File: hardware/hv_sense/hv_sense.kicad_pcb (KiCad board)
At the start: 2 copper layers, 25 parts, among them J1 Conn_01x02, J2 Conn_01x04, U1 TLV274, U2 TL431ACDT, U3 140817141410, U4 140817141410

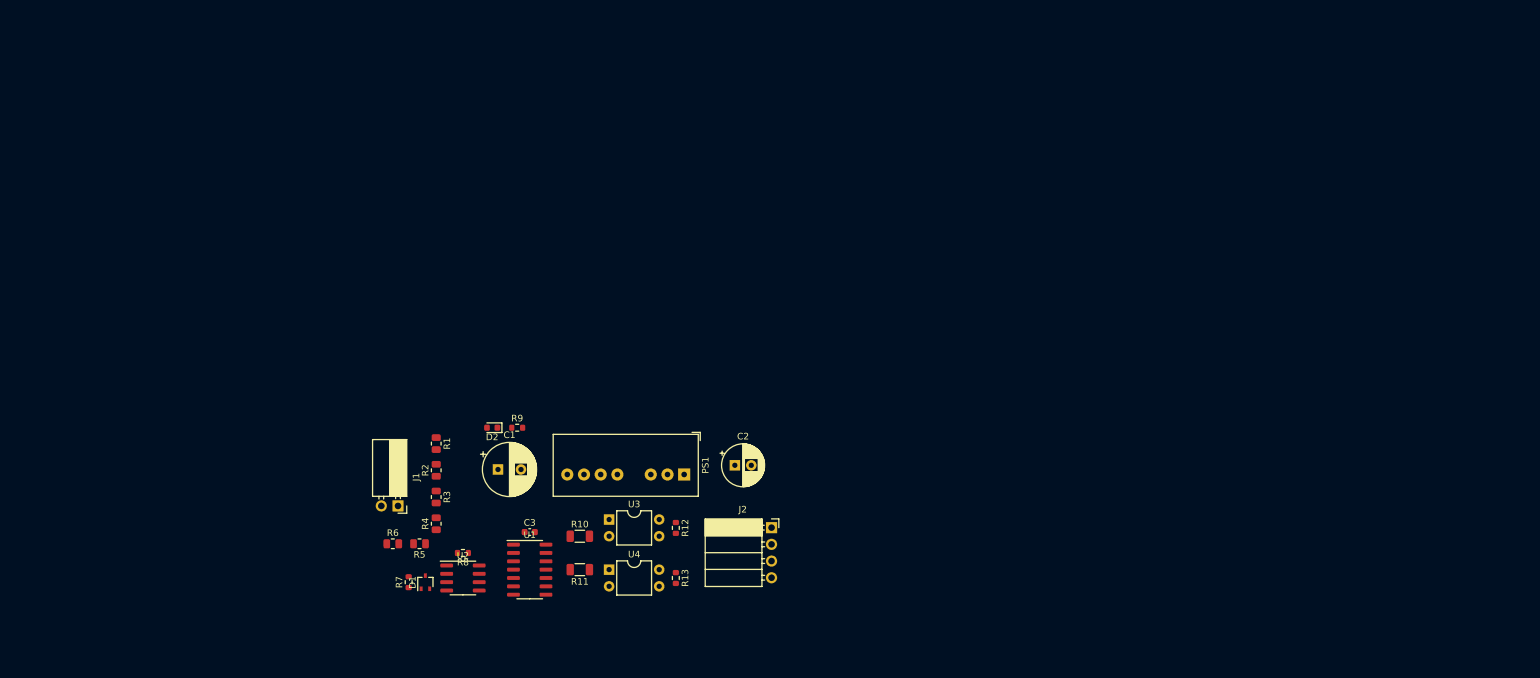
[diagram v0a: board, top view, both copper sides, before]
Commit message: Integrated TSAL logic into hv_sense
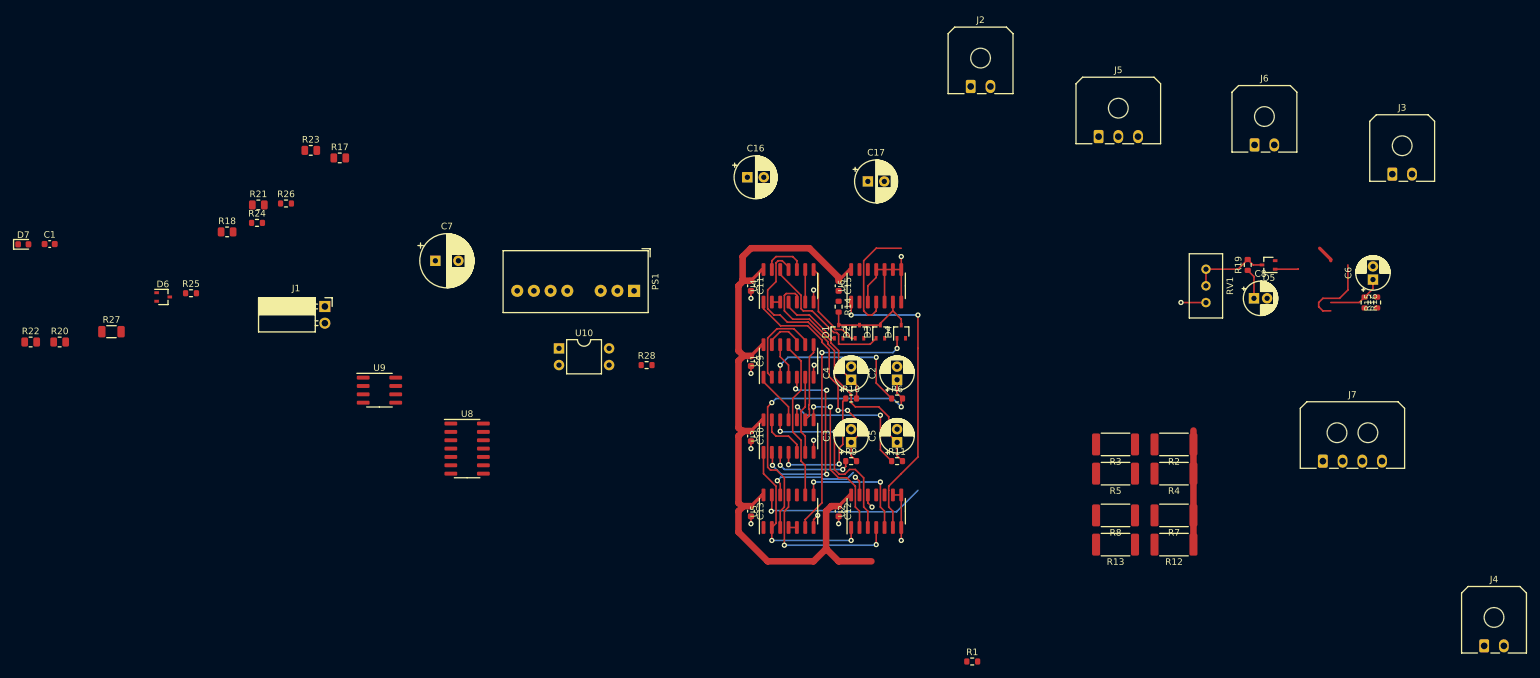
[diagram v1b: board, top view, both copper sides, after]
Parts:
- added C10: 100n, Capacitor_SMD:C_0603_1608Metric, F.Cu at (150.5, 78.1)
- added C11: 100n, Capacitor_SMD:C_0603_1608Metric, F.Cu at (150.5, 55.2)
- added C12: 100n, Capacitor_SMD:C_0603_1608Metric, F.Cu at (163.8, 89.5)
- added C13: 100n, Capacitor_SMD:C_0603_1608Metric, F.Cu at (150.5, 89.5)
- added C15: 100n, Capacitor_SMD:C_0603_1608Metric, F.Cu at (163.8, 55.2)
- added C16: 100u, Capacitor_THT:CP_Radial_D6.3mm_P2.50mm, F.Cu at (149.9, 38.7)
- added C17: 100u, Capacitor_THT:CP_Radial_D6.3mm_P2.50mm, F.Cu at (168.3, 39.4)
- added C4: 10u, Capacitor_THT:CP_Radial_D5.0mm_P2.00mm, F.Cu at (165.7, 69.5)
- added C5: 10u, Capacitor_THT:CP_Radial_D5.0mm_P2.00mm, F.Cu at (172.7, 79.1)
- added C6: 10u, Capacitor_THT:CP_Radial_D5.0mm_P2.00mm, F.Cu at (245.1, 54.3)
- added C7: 22u, Capacitor_THT:CP_Radial_D8.0mm_P3.50mm, F.Cu at (102.5, 51.4)
- added C8: 10u, Capacitor_THT:CP_Radial_D5.0mm_P2.00mm, F.Cu at (227.0, 57.1)
- added C9: 100n, Capacitor_SMD:C_0603_1608Metric, F.Cu at (150.5, 66.7)
- added D3: BAT54W, Package_TO_SOT_SMD:SOT-323_SC-70, F.Cu at (170.2, 62.2)
- added D4: BAT54W, Package_TO_SOT_SMD:SOT-323_SC-70, F.Cu at (173.4, 62.2)
- added D5: BAT54W, Package_TO_SOT_SMD:SOT-323_SC-70, F.Cu at (229.2, 52.1)
- added D6: BAT54W, Package_TO_SOT_SMD:SOT-323_SC-70, F.Cu at (61.1, 56.9)
- added D7: LED, LED_SMD:LED_0603_1608Metric, F.Cu at (39.8, 48.9)
- added J3: Conn_01x02, Connector_Molex:Molex_Micro-Fit_3.0_43650-0200_1x02_P3.00mm_Horizontal, F.Cu at (248.1, 38.3)
- added J4: Conn_01x02, Connector_Molex:Molex_Micro-Fit_3.0_43650-0200_1x02_P3.00mm_Horizontal, F.Cu at (262.0, 110.0)
- added J5: Conn_01x03, Connector_Molex:Molex_Micro-Fit_3.0_43650-0300_1x03_P3.00mm_Horizontal, F.Cu at (203.4, 32.5)
- added J6: Conn_01x02, Connector_Molex:Molex_Micro-Fit_3.0_43650-0200_1x02_P3.00mm_Horizontal, F.Cu at (227.1, 33.8)
- added J7: Conn_01x04, Connector_Molex:Molex_Micro-Fit_3.0_43650-0400_1x04_P3.00mm_Horizontal, F.Cu at (237.5, 81.9)
- added R14: 10k, Resistor_SMD:R_0603_1608Metric, F.Cu at (163.8, 58.4)
- added R15: 10k, Resistor_SMD:R_0603_1608Metric, F.Cu at (245.7, 57.8)
- added R16: 10k, Resistor_SMD:R_0603_1608Metric, F.Cu at (243.8, 57.8)
- added R17: 453k, Resistor_SMD:R_0805_2012Metric, F.Cu at (87.9, 35.8)
- added R18: 453k, Resistor_SMD:R_0805_2012Metric, F.Cu at (70.8, 47.0)
- added R19: 10k, Resistor_SMD:R_0603_1608Metric, F.Cu at (226.1, 52.1)
- added R20: 453k, Resistor_SMD:R_0805_2012Metric, F.Cu at (45.3, 63.8)
- added R21: 453k, Resistor_SMD:R_0805_2012Metric, F.Cu at (75.6, 42.9)
- added R22: 453k, Resistor_SMD:R_0805_2012Metric, F.Cu at (40.9, 63.8)
- added R23: 453k, Resistor_SMD:R_0805_2012Metric, F.Cu at (83.5, 34.6)
- added R24: 3.3k, Resistor_SMD:R_0603_1608Metric, F.Cu at (75.4, 45.7)
- added R25: 150k, Resistor_SMD:R_0603_1608Metric, F.Cu at (65.3, 56.4)
- added R26: 3.3k, Resistor_SMD:R_0603_1608Metric, F.Cu at (79.8, 42.7)
- added R27: 1k, Resistor_SMD:R_1206_3216Metric, F.Cu at (53.2, 62.2)
- added R28: 10k, Resistor_SMD:R_0603_1608Metric, F.Cu at (134.6, 67.3)
- added RV1: 470k, Potentiometer_THT:Potentiometer_Bourns_3296W_Vertical, F.Cu at (219.7, 57.8)
- added U10: 140817141410, Package_DIP:DIP-4_W7.62mm, F.Cu at (121.3, 64.8)
- added U5: 40106, Package_SO:SOIC-14_3.9x8.7mm_P1.27mm, F.Cu at (156.2, 89.5)
- added U6: 4013, Package_SO:SOIC-14_3.9x8.7mm_P1.27mm, F.Cu at (169.5, 55.2)
- added U8: TLV274, Package_SO:SOIC-14_3.9x8.7mm_P1.27mm, F.Cu at (107.3, 80.0)
- added U9: TL431ACDT, Package_SO:SOIC-8_3.9x4.9mm_P1.27mm, F.Cu at (94.0, 71.1)
- C1: value 22u -> 100n; footprint Capacitor_THT:CP_Radial_D8.0mm_P3.50mm -> Capacitor_SMD:C_0603_1608Metric
- C2: value 100u -> 10u; footprint Capacitor_THT:CP_Radial_D6.3mm_P2.50mm -> Capacitor_THT:CP_Radial_D5.0mm_P2.00mm
- C3: value 100n -> 10u; footprint Capacitor_SMD:C_0603_1608Metric -> Capacitor_THT:CP_Radial_D5.0mm_P2.00mm
- D2: value LED -> BAT54W; footprint LED_SMD:LED_0603_1608Metric -> Package_TO_SOT_SMD:SOT-323_SC-70
- J2: value Conn_01x04 -> Conn_01x02; footprint Connector_PinSocket_2.54mm:PinSocket_1x04_P2.54mm_Horizontal -> Connector_Molex:Molex_Micro-Fit_3.0_43650-0200_1x02_P3.00mm_Horizontal
- R1: value 453k -> 10k; footprint Resistor_SMD:R_0805_2012Metric -> Resistor_SMD:R_0603_1608Metric
- R10, R11: value 1k -> 10k; footprint Resistor_SMD:R_1206_3216Metric -> Resistor_SMD:R_0603_1608Metric
- R12, R13: value 10k -> 82; footprint Resistor_SMD:R_0603_1608Metric -> Resistor_SMD:R_2512_6332Metric
- R2, R3, R4, R5: value 453k -> 82; footprint Resistor_SMD:R_0805_2012Metric -> Resistor_SMD:R_2512_6332Metric
- R6: value 453k -> 100k; footprint Resistor_SMD:R_0805_2012Metric -> Resistor_SMD:R_0603_1608Metric
- R7: value 150k -> 82; footprint Resistor_SMD:R_0603_1608Metric -> Resistor_SMD:R_2512_6332Metric
- R8: value 3.3k -> 82; footprint Resistor_SMD:R_0603_1608Metric -> Resistor_SMD:R_2512_6332Metric
- R9: value 3.3k -> 10k
- U1: value TLV274 -> 4081
- U2: value TL431ACDT -> 4071; footprint Package_SO:SOIC-8_3.9x4.9mm_P1.27mm -> Package_SO:SOIC-14_3.9x8.7mm_P1.27mm
- U3: value 140817141410 -> 4081; footprint Package_DIP:DIP-4_W7.62mm -> Package_SO:SOIC-14_3.9x8.7mm_P1.27mm
- U4: value 140817141410 -> 40106; footprint Package_DIP:DIP-4_W7.62mm -> Package_SO:SOIC-14_3.9x8.7mm_P1.27mm
- moved R7 116.9 mm to (214.8, 90.2), turned to 180 degrees
- moved R4 112.5 mm to (214.8, 83.8), turned to 180 degrees
- moved R2 112.3 mm to (214.8, 79.4), turned to 180 degrees
- moved R5 106.4 mm to (206.0, 83.8)
- moved R3 103.6 mm to (206.0, 79.4), turned to 180 degrees
- moved R8 99.4 mm to (206.0, 90.2)
- moved R1 88.0 mm to (184.2, 112.4), turned to 0 degrees
- moved R6 79.8 mm to (172.7, 72.4)
- moved C1 76.3 mm to (43.8, 48.9)
- moved R12 75.8 mm to (214.8, 94.6), turned to 180 degrees
- moved J2 73.6 mm to (183.9, 24.9)
- moved D1 73.5 mm to (163.8, 62.2)
- moved R13 67.1 mm to (206.0, 94.6), turned to 180 degrees
- moved U2 63.7 mm to (169.5, 89.5), turned to 90 degrees
- moved D2 57.8 mm to (167.0, 62.2), turned to 90 degrees
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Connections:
- C2 pad 1: +12V -> Net-(C2-Pad1)
- C3 pad 1: /HV_+12V -> Net-(C3-Pad1)
- C3 pad 2: /HV_GND -> GND
- D1 pad 3: /HV_+12V -> Net-(D1-Pad3)
- D2 pad 2: /HV_+12V -> unconnected-(D2-Pad2)
- J2 pad 1: +12V -> GND
- J2 pad 2: /~{HV_PRESENT} -> /~{PRCHG_MECH_ON}
- R1 pad 1: Net-(J1-Pad2) -> /~{PRCHG_MECH_ON}
- R1 pad 2: Net-(R1-Pad2) -> +12V
- R10 pad 2: Net-(R10-Pad2) -> Net-(C4-Pad1)
- R11 pad 2: Net-(R10-Pad1) -> Net-(C5-Pad1)
- R12 pad 1: GND -> +12V
- R12 pad 2: /~{HV_PRESENT} -> Net-(R12-Pad2)
- R13 pad 1: GND -> Net-(R12-Pad2)
- R13 pad 2: /HV_PRESENT -> /~{HIGH_AIR_MECH_ON}
- R2 pad 1: Net-(R2-Pad1) -> +12V
- R2 pad 2: Net-(R1-Pad2) -> Net-(R2-Pad2)
- R3 pad 1: Net-(R2-Pad1) -> Net-(R2-Pad2)
- R3 pad 2: Net-(R3-Pad2) -> /~{LOW_AIR_MECH_ON}
- R4 pad 1: Net-(R4-Pad1) -> +12V
- R4 pad 2: Net-(R3-Pad2) -> Net-(R2-Pad2)
- R5 pad 1: Net-(R4-Pad1) -> Net-(R2-Pad2)
- R5 pad 2: Net-(R5-Pad2) -> /~{LOW_AIR_MECH_ON}
- R6 pad 1: Net-(D1-Pad1) -> Net-(R6-Pad1)
- R6 pad 2: Net-(R5-Pad2) -> Net-(C2-Pad1)
- R7 pad 1: Net-(D1-Pad1) -> +12V
- R7 pad 2: /HV_GND -> Net-(R12-Pad2)
- R8 pad 1: /HV_+12V -> Net-(R12-Pad2)
- R8 pad 2: /VREF_2.5V -> /~{HIGH_AIR_MECH_ON}
- R9 pad 1: Net-(D2-Pad1) -> Net-(R9-Pad1)
- R9 pad 2: /HV_GND -> Net-(C3-Pad1)
- U1 pad 1: Net-(R10-Pad1) -> Net-(U1-Pad1)
- U1 pad 10: /HV_GND -> Net-(U1-Pad10)
- U1 pad 11: /HV_GND -> Net-(U1-Pad11)
- U1 pad 12: /HV_GND -> Net-(U1-Pad12)
- U1 pad 13: /HV_+12V -> Net-(U1-Pad10)
- U1 pad 14: unconnected-(U1-Pad14) -> +12V
- U1 pad 2: /VREF_2.5V -> /~{HV_DETECTED}
- U1 pad 3: Net-(D1-Pad1) -> Net-(R6-Pad1)
- U1 pad 4: /HV_+12V -> Net-(U1-Pad12)
- U1 pad 5: /HV_GND -> /~{PRCHG_MECH_ON}
- U1 pad 6: /HV_+12V -> /~{LOW_AIR_MECH_ON}
- U1 pad 7: unconnected-(U1-Pad7) -> GND
- U1 pad 8: unconnected-(U1-Pad8) -> /~{HIGH_AIR_MECH_ON}
- U1 pad 9: /HV_+12V -> /~{HV_DETECTED}
- U2 pad 1: /VREF_2.5V -> /PRCHG_INTENDED_ON
- U2 pad 2: /HV_GND -> /HIGH_AIR_INTENDED_ON
- U2 pad 3: /HV_GND -> Net-(U2-Pad3)
- U2 pad 4: (no net) -> Net-(U2-Pad4)
- U2 pad 5: (no net) -> /Implausibility and LED logic/TS_UNSAFE
- U2 pad 6: /HV_GND -> /Implausibility and LED logic/IMPLAUSIBLE
- U2 pad 7: /HV_GND -> GND
- U2 pad 8: /VREF_2.5V -> GND
- U3 pad 1: /HV_+12V -> /PRCHG_INTENDED_ON
- U3 pad 2: Net-(R10-Pad2) -> /~{PRCHG_MECH_ON}
- U3 pad 3: /~{HV_PRESENT} -> Net-(R9-Pad1)
- U3 pad 4: +12V -> Net-(R10-Pad1)
- U4 pad 1: Net-(R11-Pad1) -> Net-(C3-Pad1)
- U4 pad 2: /HV_GND -> Net-(U4-Pad2)
- U4 pad 3: /HV_PRESENT -> Net-(U4-Pad2)
- U4 pad 4: +12V -> Net-(D1-Pad1)
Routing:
- net +12V: track 0.00 -> 133.7 mm
- net GND: track 0.00 -> 47.7 mm, vias 0 -> 13
- net /Implausibility and LED logic/IMPLAUSIBLE: track 0.00 -> 46.6 mm, vias 0 -> 2
- net Net-(C5-Pad1): track 0.00 -> 46.5 mm
- net Net-(C2-Pad1): track 0.00 -> 46.1 mm, vias 0 -> 2
- net /Implausibility and LED logic/POR: track 0.00 -> 44.3 mm, vias 0 -> 1
- net Net-(D4-Pad1): track 0.00 -> 40.9 mm, vias 0 -> 2
- net Net-(C6-Pad1): track 0.00 -> 35.0 mm, vias 0 -> 1
- net Net-(C3-Pad1): track 0.00 -> 34.3 mm, vias 0 -> 2
- net /~{PRCHG_MECH_ON}: track 0.00 -> 30.4 mm, vias 0 -> 4
- net Net-(U2-Pad3): track 0.00 -> 29.3 mm, vias 0 -> 2
- net /PRCHG_INTENDED_ON: track 0.00 -> 28.5 mm, vias 0 -> 2
- net /HIGH_AIR_INTENDED_ON: track 0.00 -> 25.4 mm, vias 0 -> 2
- net Net-(U1-Pad11): track 0.00 -> 25.0 mm
- net Net-(C4-Pad1): track 0.00 -> 24.9 mm
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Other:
- board text added: "100u"

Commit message: Begun routing hv_sense
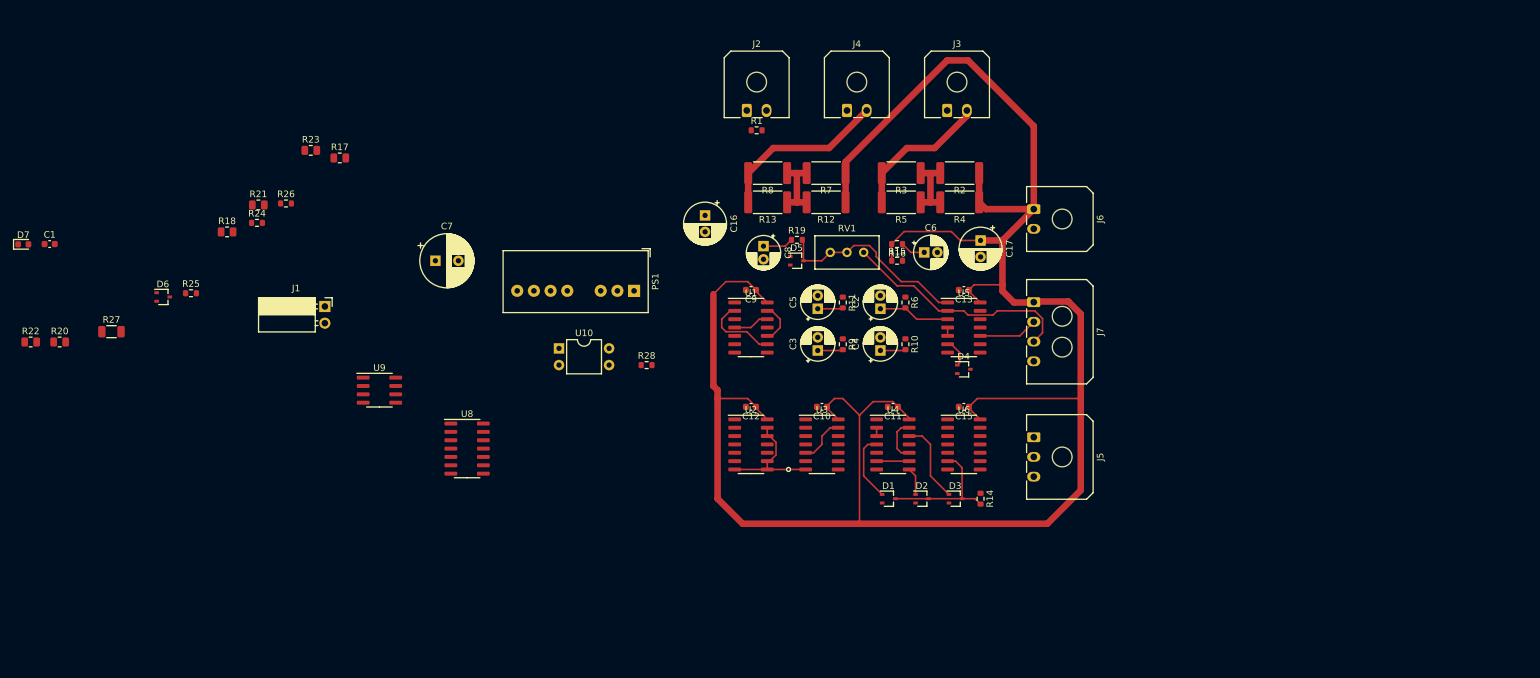
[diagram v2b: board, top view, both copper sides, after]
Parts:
- moved J4 126.6 mm to (165.1, 28.6)
- moved R1 87.2 mm to (151.4, 31.6)
- moved C8 75.0 mm to (152.4, 49.2), turned to -90 degrees
- moved R7 74.2 mm to (161.9, 38.1)
- moved R8 74.2 mm to (153.0, 38.1)
- moved R12 74.2 mm to (161.9, 42.5)
- moved R13 74.2 mm to (153.0, 42.5)
- moved R15 73.3 mm to (172.7, 51.4), turned to 0 degrees
- moved D5 71.8 mm to (157.5, 51.4), turned to 0 degrees
- moved R16 71.7 mm to (172.7, 48.9), turned to 180 degrees
- moved R19 68.7 mm to (157.5, 48.3), turned to 0 degrees
- moved J3 68.4 mm to (180.3, 28.6)
- moved C6 68.4 mm to (176.8, 50.2), turned to 0 degrees
- moved RV1 52.6 mm to (167.6, 50.2), turned to 0 degrees
- moved R2 52.6 mm to (182.2, 38.1)
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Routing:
- net +12V: track 133.7 -> 319.9 mm
- net /Implausibility and LED logic/IMPLAUSIBLE: track 46.6 -> 0.00 mm, vias 2 -> 0
- net /Implausibility and LED logic/POR: track 44.3 -> 0.00 mm, vias 1 -> 0
- net Net-(C5-Pad1): track 46.5 -> 3.86 mm
- net Net-(D4-Pad1): track 40.9 -> 4.41 mm, vias 2 -> 0
- net Net-(C2-Pad1): track 46.1 -> 11.0 mm, vias 2 -> 0
- net /Implausibility and LED logic/RED_LED_ON: track 4.07 -> 36.0 mm, vias 1 -> 0
- net Net-(C6-Pad1): track 35.0 -> 3.83 mm, vias 1 -> 0
- net /~{PRCHG_MECH_ON}: track 30.4 -> 0.00 mm, vias 4 -> 0
- net Net-(C3-Pad1): track 34.3 -> 3.86 mm, vias 2 -> 0
- net Net-(U2-Pad3): track 29.3 -> 0.00 mm, vias 2 -> 0
- net GND: track 47.7 -> 18.7 mm, vias 13 -> 1
- net /PRCHG_INTENDED_ON: track 28.5 -> 0.00 mm, vias 2 -> 0
- net /HIGH_AIR_INTENDED_ON: track 25.4 -> 0.00 mm, vias 2 -> 0
- net Net-(U1-Pad11): track 25.0 -> 0.00 mm
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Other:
- board text removed: "100u"

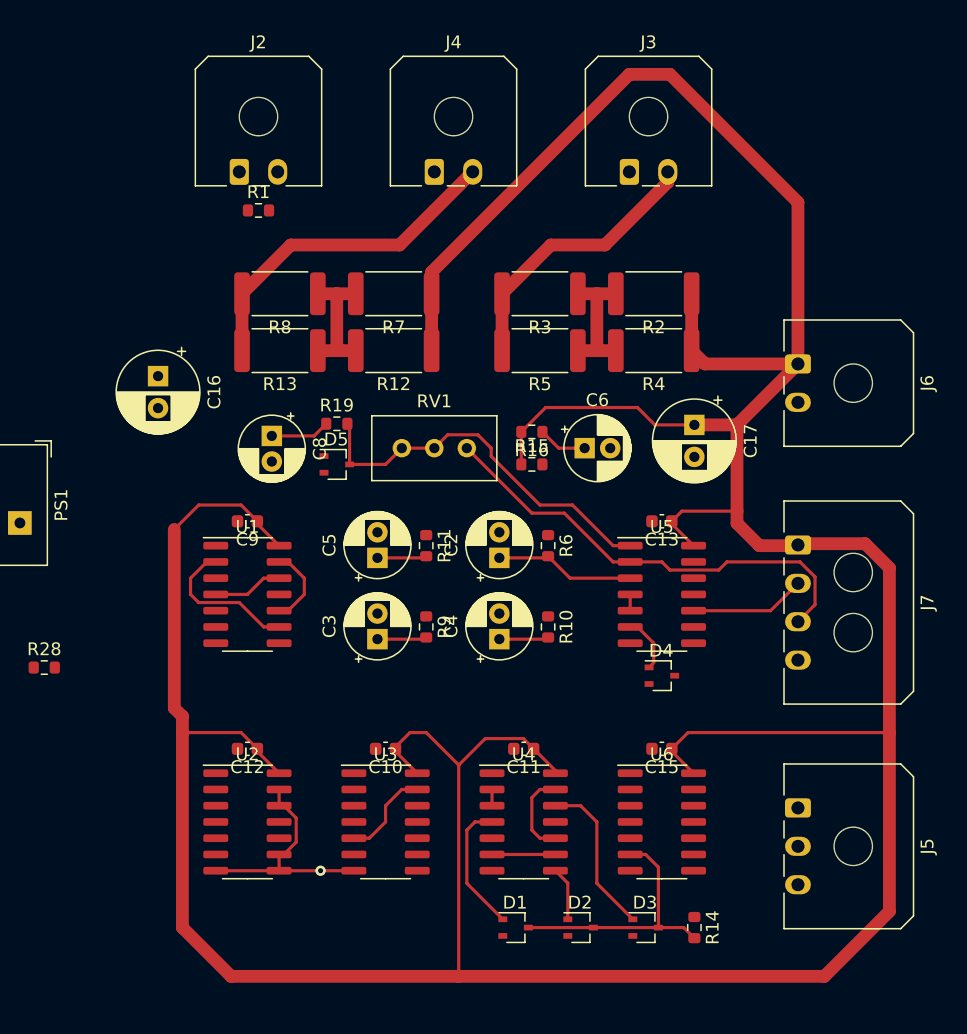
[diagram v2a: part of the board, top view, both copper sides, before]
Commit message: Routed LV side of hv_sense
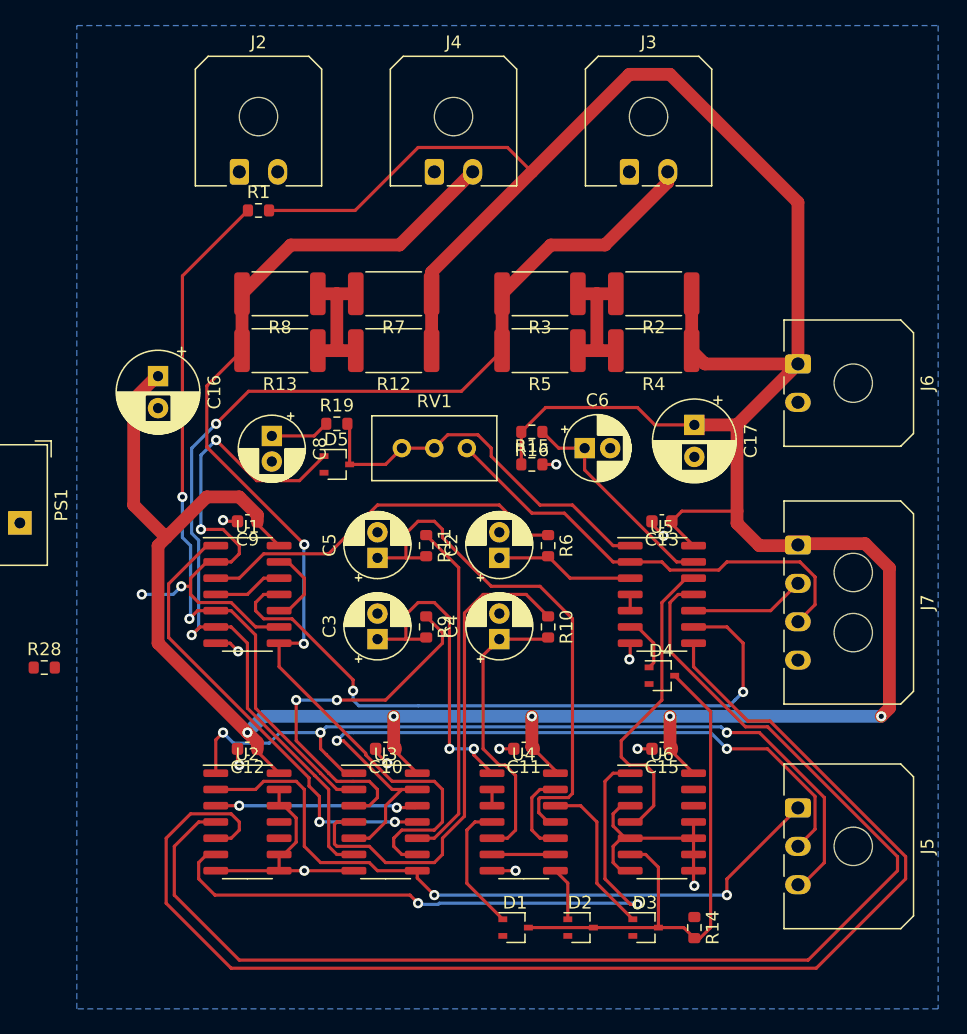
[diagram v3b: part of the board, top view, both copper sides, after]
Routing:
- net /Implausibility and LED logic/TS_UNSAFE: track 0.00 -> 103.7 mm
- net Net-(U2-Pad4): track 0.00 -> 100.8 mm
- net /~{LOW_AIR_MECH_ON}: track 21.8 -> 90.2 mm, vias 0 -> 2
- net /PRCHG_INTENDED_ON: track 0.00 -> 66.1 mm, vias 0 -> 3
- net /~{HIGH_AIR_MECH_ON}: track 26.4 -> 83.8 mm, vias 0 -> 2
- net /~{PRCHG_MECH_ON}: track 0.00 -> 56.6 mm, vias 0 -> 2
- net /HIGH_AIR_INTENDED_ON: track 0.00 -> 55.9 mm, vias 0 -> 2
- net Net-(U1-Pad11): track 0.00 -> 53.5 mm, vias 0 -> 2
- net /Implausibility and LED logic/IMPLAUSIBLE: track 0.00 -> 51.3 mm, vias 0 -> 2
- net /LOW_AIR_INTENDED_ON: track 7.27 -> 58.1 mm, vias 0 -> 2
- net +12V: track 319.9 -> 278.1 mm, vias 0 -> 5
- net Net-(R10-Pad1): track 0.00 -> 39.9 mm
- net Net-(C5-Pad1): track 3.86 -> 41.8 mm
- net Net-(U1-Pad1): track 0.00 -> 36.1 mm, vias 0 -> 2
- net GND: track 18.7 -> 51.4 mm, vias 1 -> 12
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- added copper zone on B.Cu, net GND

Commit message: Routing done, still needs finishing touches though
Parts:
- J1: footprint Connector_PinSocket_2.54mm:PinSocket_1x02_P2.54mm_Horizontal -> Connector_Molex:Molex_Micro-Fit_3.0_43650-0200_1x02_P3.00mm_Horizontal
- moved C1 81.0 mm to (122.6, 67.9), turned to 180 degrees
- moved D7 80.9 mm to (119.4, 34.3), turned to 90 degrees
- moved R22 70.4 mm to (109.9, 78.1), turned to -90 degrees
- moved R27 69.4 mm to (122.6, 65.4)
- moved D6 65.9 mm to (122.6, 80.6)
- moved R20 64.9 mm to (109.9, 70.5), turned to -90 degrees
- moved R25 57.2 mm to (116.8, 81.3)
- moved R23 55.2 mm to (113.0, 81.3), turned to 180 degrees
- moved R24 48.2 mm to (122.6, 55.2), turned to 180 degrees
- moved R21 46.5 mm to (109.9, 74.3), turned to 90 degrees
- moved R18 43.7 mm to (109.9, 66.7), turned to 90 degrees
- moved R26 40.0 mm to (119.4, 37.5), turned to -90 degrees
- moved R17 34.8 mm to (109.9, 62.9), turned to -90 degrees
- moved U9 31.0 mm to (122.6, 59.1)
- moved J1 28.3 mm to (113.8, 55.5), turned to 90 degrees
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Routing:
- net /HV_+12V: track 0.00 -> 88.6 mm
- net /HV_GND: track 0.00 -> 79.9 mm, vias 0 -> 2
- net /VREF_2.5V: track 0.00 -> 27.1 mm, vias 0 -> 2
- net Net-(D6-Pad1): track 0.00 -> 19.3 mm
- net +12V: track 278.1 -> 294.1 mm
- net Net-(J1-Pad2): track 0.00 -> 11.1 mm
- net /~{HV_DETECTED}: track 40.1 -> 48.0 mm
- net Net-(R27-Pad2): track 0.00 -> 6.69 mm
- net Net-(R27-Pad1): track 0.00 -> 4.86 mm
- net Net-(R22-Pad2): track 0.00 -> 3.20 mm
- net Net-(R21-Pad1): track 0.00 -> 1.98 mm
- net Net-(R20-Pad2): track 0.00 -> 1.98 mm
- net Net-(R18-Pad1): track 0.00 -> 1.98 mm
- net Net-(R17-Pad2): track 0.00 -> 1.98 mm
- net Net-(D7-Pad1): track 0.00 -> 1.56 mm
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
